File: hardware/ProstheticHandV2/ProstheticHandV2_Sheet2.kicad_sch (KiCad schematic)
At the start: 30 parts, among them SW2 BUTTON_01, SW4 BUTTON_02

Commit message: Started working on PCB
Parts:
- added H1, H2, H3, H4: MountingHole, MountingHole:MountingHole_3.2mm_M3, symbol Mechanical:MountingHole
- C10: renamed from C15; footprint (none) -> Capacitor_THT:C_Disc_D3.8mm_W2.6mm_P2.50mm
- C11: renamed from C13; footprint (none) -> Capacitor_THT:C_Disc_D3.8mm_W2.6mm_P2.50mm
- C7: renamed from C11; footprint (none) -> Capacitor_THT:C_Disc_D3.8mm_W2.6mm_P2.50mm
- C8: renamed from C7; footprint (none) -> Capacitor_THT:C_Disc_D3.8mm_W2.6mm_P2.50mm
- C9: footprint (none) -> Capacitor_THT:C_Disc_D3.8mm_W2.6mm_P2.50mm
- R13: renamed from R14; footprint (none) -> Resistor_THT:R_Axial_DIN0207_L6.3mm_D2.5mm_P7.62mm_Horizontal
- R14: renamed from R17; footprint (none) -> Resistor_THT:R_Axial_DIN0207_L6.3mm_D2.5mm_P7.62mm_Horizontal
- R15: renamed from R21; footprint (none) -> Resistor_THT:R_Axial_DIN0207_L6.3mm_D2.5mm_P7.62mm_Horizontal
- R16: renamed from R19; footprint (none) -> Resistor_THT:R_Axial_DIN0207_L6.3mm_D2.5mm_P7.62mm_Horizontal
- R17: renamed from R23; footprint (none) -> Resistor_THT:R_Axial_DIN0207_L6.3mm_D2.5mm_P7.62mm_Horizontal
- R18: renamed from R25; footprint (none) -> Resistor_THT:R_Axial_DIN0207_L6.3mm_D2.5mm_P7.62mm_Horizontal
- R3: footprint (none) -> Resistor_THT:R_Axial_DIN0207_L6.3mm_D2.5mm_P7.62mm_Horizontal
- RV1: footprint (none) -> Potentiometer_THT:Potentiometer_Alps_RK163_Dual_Horizontal
- RV2, RV3: footprint (none) -> Potentiometer_THT:Potentiometer_Bourns_3296W_Vertical
- SW2: footprint (none) -> Button_Switch_THT:SW_PUSH_6mm_H5mm
- SW3: renamed from SW4; footprint (none) -> Button_Switch_THT:SW_PUSH_6mm_H5mm
- TP3: footprint (none) -> TestPoint:TestPoint_Pad_D2.5mm
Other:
- note added: "Mounting holes"

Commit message: Finalize PCB design for china
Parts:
- removed H1, H2, H3, H4: MountingHole, MountingHole:MountingHole_3.2mm_M3, symbol Mechanical:MountingHole
- added H1, H2, H3, H4: MountingHole_Pad, MountingHole:MountingHole_3.2mm_M3_Pad, symbol Mechanical:MountingHole_Pad
- renumbered C9 to C10, C10 to C11, C11 to C8, C8 to C9, R13 to R10, R16 to R12, R17 to R13, R14 to R15, R15 to R17
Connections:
- net GND: now also H1.1, H2.1, H3.1, H4.1

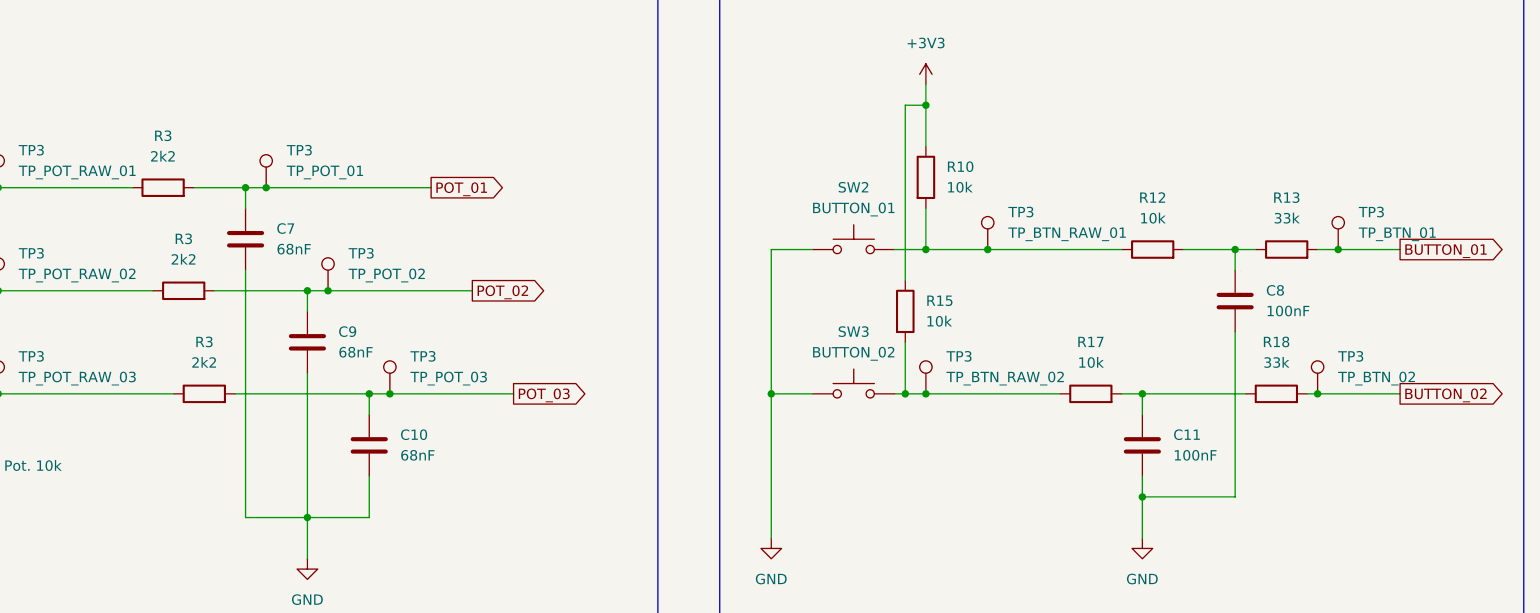
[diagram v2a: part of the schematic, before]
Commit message: Update PCB, sent to JLCPCB
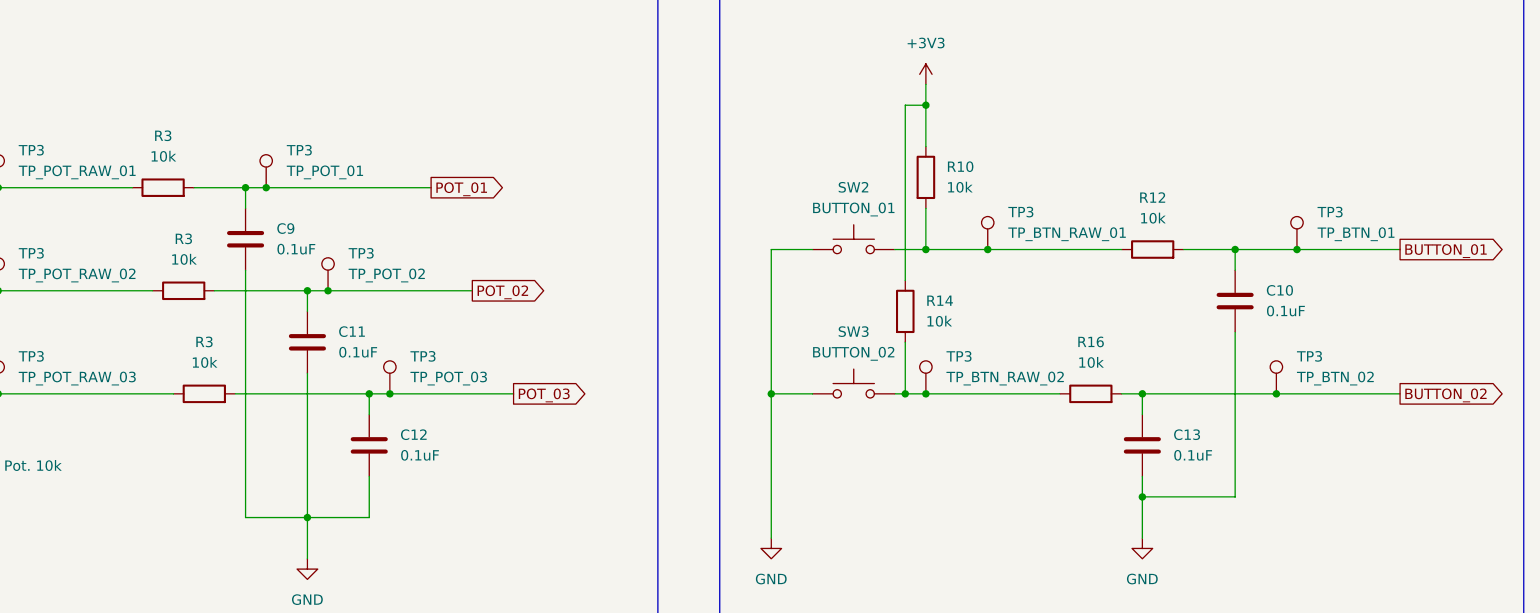
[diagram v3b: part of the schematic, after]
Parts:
- removed R13, R18: 33k, Resistor_THT:R_Axial_DIN0207_L6.3mm_D2.5mm_P7.62mm_Horizontal, symbol Device:R
- C10: renamed from C8; value 100nF -> 0.1uF; footprint Capacitor_THT:C_Disc_D3.8mm_W2.6mm_P2.50mm -> Capacitor_SMD:C_1206_3216Metric
- C11: renamed from C9; value 68nF -> 0.1uF; footprint Capacitor_THT:C_Disc_D3.8mm_W2.6mm_P2.50mm -> Capacitor_SMD:C_1206_3216Metric
- C12: renamed from C10; value 68nF -> 0.1uF; footprint Capacitor_THT:C_Disc_D3.8mm_W2.6mm_P2.50mm -> Capacitor_SMD:C_1206_3216Metric
- C13: renamed from C11; value 100nF -> 0.1uF; footprint Capacitor_THT:C_Disc_D3.8mm_W2.6mm_P2.50mm -> Capacitor_SMD:C_1206_3216Metric
- C9: renamed from C7; value 68nF -> 0.1uF; footprint Capacitor_THT:C_Disc_D3.8mm_W2.6mm_P2.50mm -> Capacitor_SMD:C_1206_3216Metric
- R10, R12: footprint Resistor_THT:R_Axial_DIN0207_L6.3mm_D2.5mm_P7.62mm_Horizontal -> Resistor_SMD:R_1206_3216Metric
- R14: renamed from R15; footprint Resistor_THT:R_Axial_DIN0207_L6.3mm_D2.5mm_P7.62mm_Horizontal -> Resistor_SMD:R_1206_3216Metric
- R16: renamed from R17; footprint Resistor_THT:R_Axial_DIN0207_L6.3mm_D2.5mm_P7.62mm_Horizontal -> Resistor_SMD:R_1206_3216Metric
- R3: value 2k2 -> 10k; footprint Resistor_THT:R_Axial_DIN0207_L6.3mm_D2.5mm_P7.62mm_Horizontal -> Resistor_SMD:R_1206_3216Metric
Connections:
- net BUTTON_01: now also C10.1, R12.2
- net BUTTON_02: now also C13.1, R16.2
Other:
- moved on the sheet: TP3
